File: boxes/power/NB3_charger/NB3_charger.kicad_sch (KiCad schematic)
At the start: 58 parts, among them J1 Barrel_Jack-DC-5.5-2.1, J2 B4B-PH-K-S, J3 Conn_01x02_Pin, J4 Conn_01x02_Pin, J5 Conn_01x02_Pin, J6 Conn_01x02_Pin, Q1 PMOS_FDC658AP, SW1 SW_SPDT, SW2 SW_SPDT, T1 NTCG163JF103FT1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

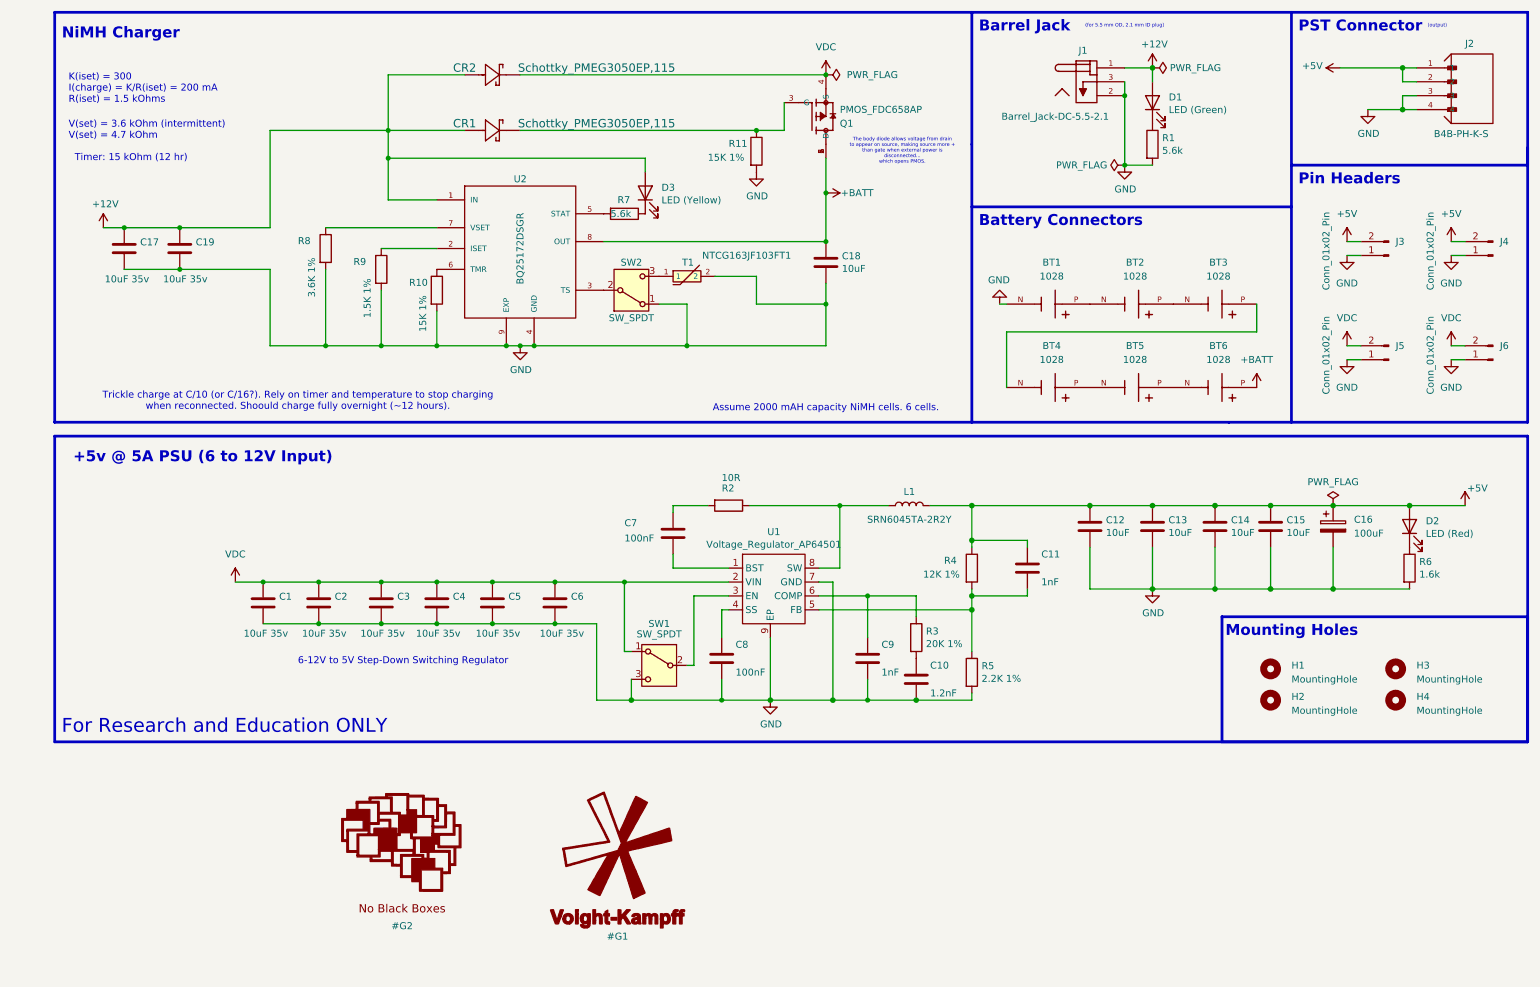
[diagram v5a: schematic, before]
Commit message: Work on NB3 charger PCB layout
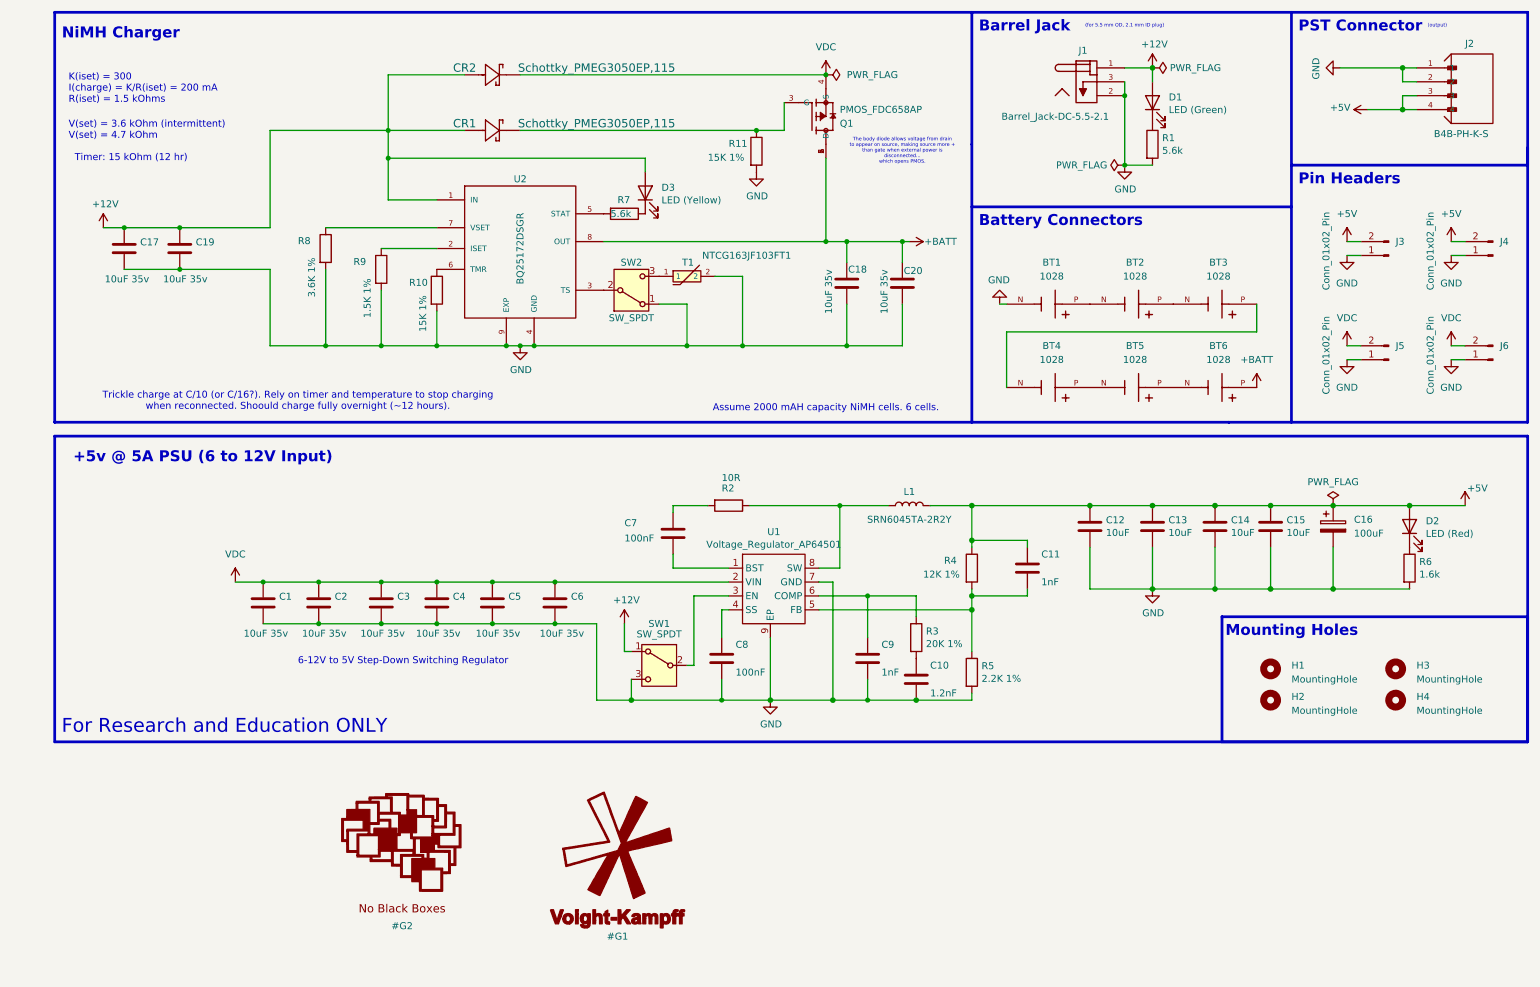
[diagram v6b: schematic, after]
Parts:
- added C20: 10uF 35v, Capacitor_SMD:C_0805_2012Metric, symbol Device:C
- C18: value 10uF -> 10uF 35v; Field5 490-14381-1-ND -> 490-10505-1-ND; Field6 GRM21BR71A106KA73L -> GRM21BC8YA106KE11L; Field8 111893011 -> (none); Part Description 10uF 10% 10V Ceramic Capacitor X7R 0805 (2012 Metric) -> 10uF 10% or 20% 35V Ceramic Capacitor X6S 0805 (2012 Metric)
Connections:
- net +12V: now also SW1.1 (A)
- net +5V: now also J2.3, J2.4; no longer J2.1, J2.2
- net +BATT: now also C20.1
- net GND: now also J2.1, J2.2, C20.2; no longer J2.3, J2.4
- net VDC: no longer SW1.1 (A)

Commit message: Finish draft of NB3 Charger (submitted for Fab)
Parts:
- BT1, BT2, BT3, BT4, BT5, BT6: footprint NB3_charger:AA_Battery_Holder_1028 -> NB3_charger:AA_Battery_Holder_BH-AA-A5BJ012; symbol NB3_charger:AA_Battery_Holder_1028 -> NB3_charger:AA_Battery_Holder_BH-AA-A5BJ012; LCSC (none) -> C5290180
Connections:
- net +BATT: now also BT6.1; no longer BT6.P
- net GND: now also BT1.2; no longer BT1.N
- new net: BT3.1, BT4.2
- new net: BT2.1, BT3.2
- new net: BT4.1, BT5.2
- new net: BT5.1, BT6.2
- new net: BT1.1, BT2.2
